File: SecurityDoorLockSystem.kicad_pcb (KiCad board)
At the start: 2 copper layers, 79.3 x 65.1 mm, 9 parts, among them J1 Power In, J2 Servo, J3 RFID-RC522, J4 R307s, U1 ESP32-DEVKIT-V1

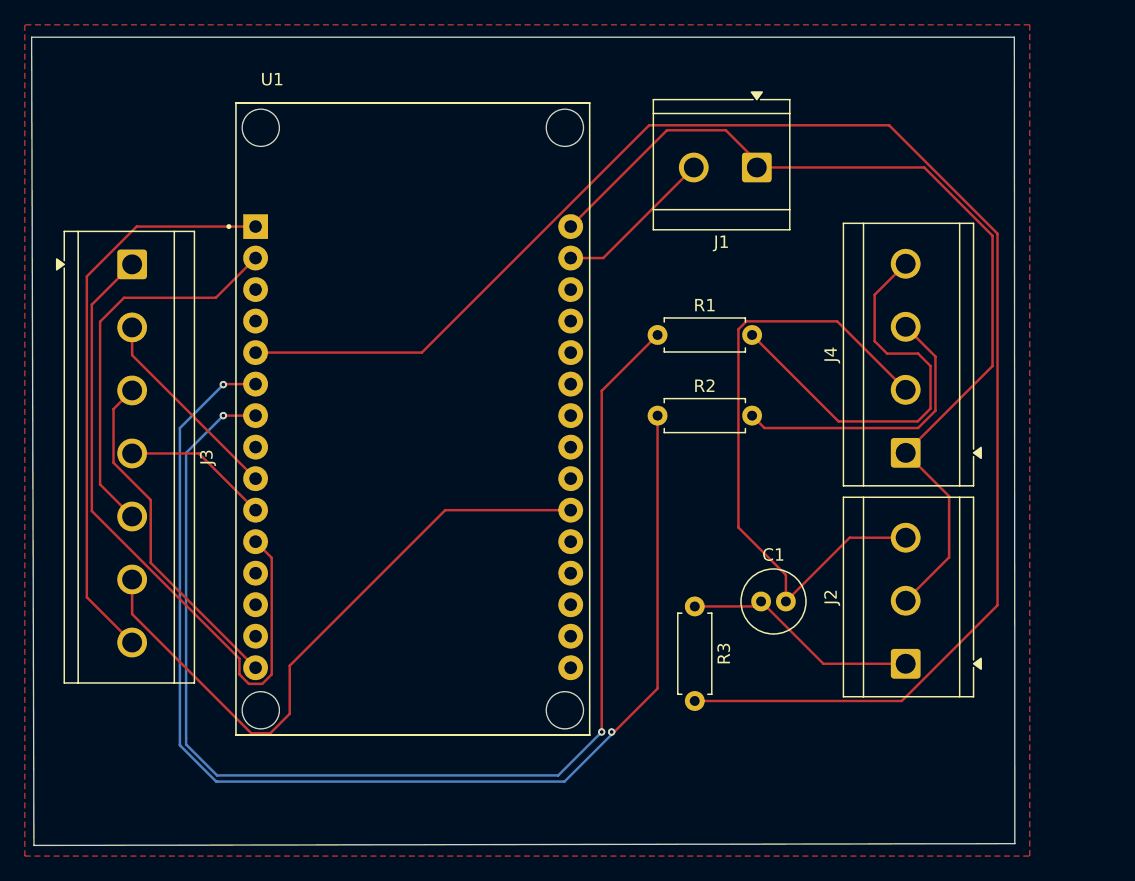
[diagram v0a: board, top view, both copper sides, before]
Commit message: version 2
increased track width
added voltage regulator
corrected tht-friendly error
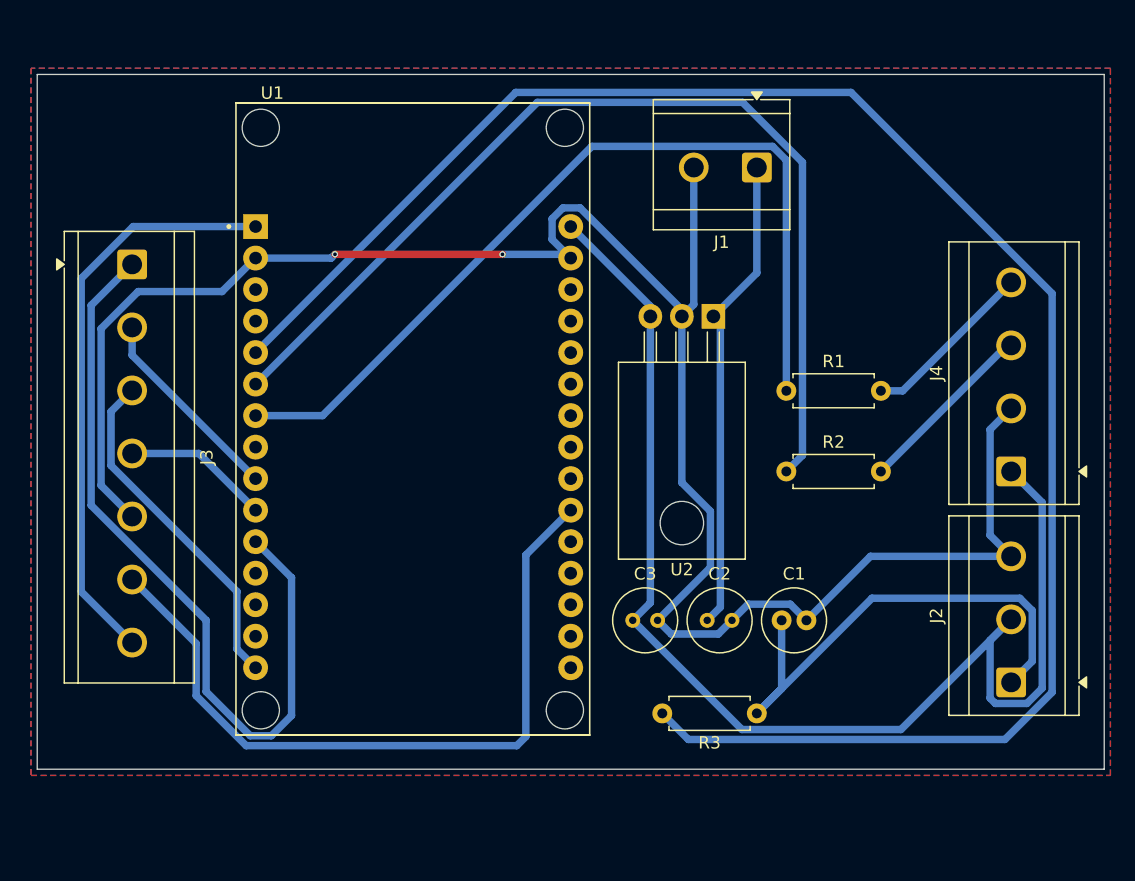
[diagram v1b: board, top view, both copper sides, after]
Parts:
- added C2: C, Capacitor_THT:C_Radial_D5.0mm_H7.0mm_P2.00mm, F.Cu at (142.0, 97.0)
- added C3: C, Capacitor_THT:C_Radial_D5.0mm_H7.0mm_P2.00mm, F.Cu at (136.0, 97.0)
- added U2: L7805, Package_TO_SOT_THT:TO-220-3_Horizontal_TabDown, F.Cu at (142.5, 72.5)
- moved R1 11.3 mm to (148.4, 78.5)
- moved R2 11.3 mm to (148.4, 85.0)
- moved R3 9.97 mm to (146.0, 104.5), turned to 180 degrees
- moved J2 8.63 mm to (166.5, 102.0)
- moved J4 8.63 mm to (166.5, 85.0)
- moved C1 2.25 mm to (148.0, 97.0)
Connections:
- J1 pad 1: VCC -> /VCC
- J2 pad 2: VCC -> /5V
- J4 pad 1: VCC -> /5V
- U1 pad 30: VCC -> /5V
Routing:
- net /5V: track 0.00 -> 103.3 mm
- net VCC: track 76.2 -> 0.00 mm
- net GND: track 96.5 -> 160.8 mm, vias 0 -> 2
- net /VCC: track 0.00 -> 38.6 mm
- net Net-(U1-TX2): track 100.2 -> 70.8 mm, vias 2 -> 0
- net /Servo Signal: track 19.2 -> 41.3 mm
- net /Transmitter: track 33.7 -> 14.1 mm
- net Net-(U1-RX2): track 98.1 -> 80.9 mm, vias 2 -> 0
- net Net-(U1-D4): track 128.6 -> 145.6 mm
- net /SDA: track 53.8 -> 63.9 mm
- net /Receiver: track 23.5 -> 14.7 mm
- net /RST: track 51.8 -> 59.8 mm
- net /3v3: track 46.3 -> 46.8 mm
- added copper zone on B.Cu, net GND
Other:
- board size 79.3 x 65.1 mm -> 86 x 56 mm
